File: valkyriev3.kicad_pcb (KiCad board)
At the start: 4 copper layers, 70 x 100 mm, 126 parts, among them J1 USB_C_Receptacle_USB2.0_16P, J10 Conn_01x03, J11 Conn_01x03, J2 DE9_Pins_MountingHoles, J3 SMA_180C, J4 SMA_180C, J5 Conn_01x02_Socket, J6 Conn_01x02_Socket, J7 Conn_01x02_Socket, J8 Conn_01x03, J9 Conn_01x05, Q1 BC817, Q2 BC817, Q3 BC817, Q4 BC817, Q5 BC817, Q6 DMG3420U, Q7 DMP2305U, Q8 DMG3420U, SW1 SW_SPST, SW2 SW_SPST, U1 W25Q128JVS, U10 LPS22HB, U2 ESP32-S3-MINI-1U, U3 MAX3232, U4 AMS1117-3.3, U5 TPS562202, U9 MS5607-02BA

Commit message: did some clean-up, did some to-do tasks.
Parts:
- added D1: S2A, Diode_SMD:D_SMB, B.Cu at (110.5, 89.7)
- added Q6: BC817, Package_TO_SOT_SMD:SOT-23, F.Cu at (136.5, 88.1)
- added Q7: BC817, Package_TO_SOT_SMD:SOT-23, F.Cu at (134.9, 91.5)
- added R24: 1k, Resistor_SMD:R_0603_1608Metric, F.Cu at (137.0, 85.6)
- added R25: 1k, Resistor_SMD:R_0603_1608Metric, F.Cu at (133.8, 87.9)
- added R26: 1k, Resistor_SMD:R_0603_1608Metric, F.Cu at (137.6, 91.3)
- added R27: 1k, Resistor_SMD:R_0603_1608Metric, F.Cu at (132.2, 90.5)
- moved J4 16.0 mm to (162.0, 114.1)
- moved J9 4.45 mm to (136.0, 95.2)
- renumbered D9 to D10, D10 to D11, D11 to D12, D1 to D2, D2 to D3, D3 to D4, D4 to D5, D5 to D6, D6 to D7, D7 to D8, D8 to D9, Q8 to Q10, Q6 to Q8, Q7 to Q9, R24 to R28, R25 to R29, R26 to R30, R27 to R31, R28 to R32
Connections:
- J1 pad A4: +5V -> /MCU/USB_VBUS
- J1 pad A9: +5V -> /MCU/USB_VBUS
- J1 pad B4: +5V -> /MCU/USB_VBUS
- J1 pad B9: +5V -> /MCU/USB_VBUS
- U2 pad 19: LORA_M0 -> LORA_M1
- U2 pad 20: LORA_M1 -> LORA_M0
- U2 pad 36: ESP_TXD2 -> ESP_RXD2
- U2 pad 37: ESP_RXD2 -> ESP_TXD2
- U8 pad 4: ESP_TXD1 -> ESP_RXD1
- U8 pad 5: ESP_RXD1 -> ESP_TXD1
- U8 pad 6: LORA_M0 -> /Communications/LORA_M1_C
- U8 pad 7: LORA_M1 -> /Communications/LORA_M0_C
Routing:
- net /MCU/USB_VBUS: track 0.00 -> 17.9 mm, vias 0 -> 8
- net +5V: track 92.3 -> 74.8 mm, vias 23 -> 15
- net /Communications/LORA_ANT: track 6.85 -> 20.5 mm
- net ESP_RXD1: track 50.6 -> 62.7 mm
- net LORA_M0: track 31.2 -> 20.7 mm, vias 2 -> 0
- net /Communications/LORA_M0_C: track 0.00 -> 10.3 mm
- net ESP_TXD1: track 50.3 -> 57.3 mm
- net /Communications/LORA_M1_C: track 0.00 -> 6.42 mm
- net LORA_M1: track 30.2 -> 24.2 mm, vias 2 -> 0
- net +3V3: track 38.8 -> 41.3 mm, vias 62 -> 64
- net /Communications/LORA_M0_B: track 0.00 -> 2.11 mm
- net /Communications/LORA_M1_B: track 0.00 -> 1.81 mm
- net ESP_RXD2: track 44.8 -> 44.5 mm, vias 2 -> 0
- net GND: vias 379 -> 398

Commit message: improvements, re-did some tasks. updated step file.
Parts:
- D1: value S2A -> 1N4007; footprint Diode_SMD:D_SMB -> Diode_THT:D_DO-41_SOD81_P2.54mm_Vertical_AnodeUp; moved to F.Cu
- moved G*** 2.74 mm to (153.3, 114.0)
- moved D1 0.77 mm to (109.7, 89.6)
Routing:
- net +5V: track 74.8 -> 78.6 mm
- net BUZZER: track 16.2 -> 18.1 mm
- net /MCU/ESP_BOOT: track 17.2 -> 18.5 mm
- net /MCU/USB_VBUS: track 17.9 -> 17.0 mm
- net GND: vias 398 -> 397
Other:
- board text added: "Designed By S. KÖMÜRCÜOĞLU"
- board text added: "GUNALTAY ROCKET TEAM Valkyrie V3.1 Flight Computer"
- board text added: "GUNALTAY ROCKET TEAM Valkyrie V3.1 Flight Computer Drawn By: S. KÖMÜRCÜOĞLU Reviewed By: Ö.T. ÖNSOY VIN: 7-15V DC"
- board text removed: "Drawn by S. KÖMÜRCÜOĞLU"
- board text removed: "GUNALTAY ROCKET TEAM Valkyrie V3 Flight Computer"
- board text removed: "GUNALTAY ROCKET TEAM Valkyrie V3 Flight Computer Drawn By: S. KÖMÜRCÜOĞLU Reviewed By: Ö.T. ÖNSOY VIN: 7-15V DC"

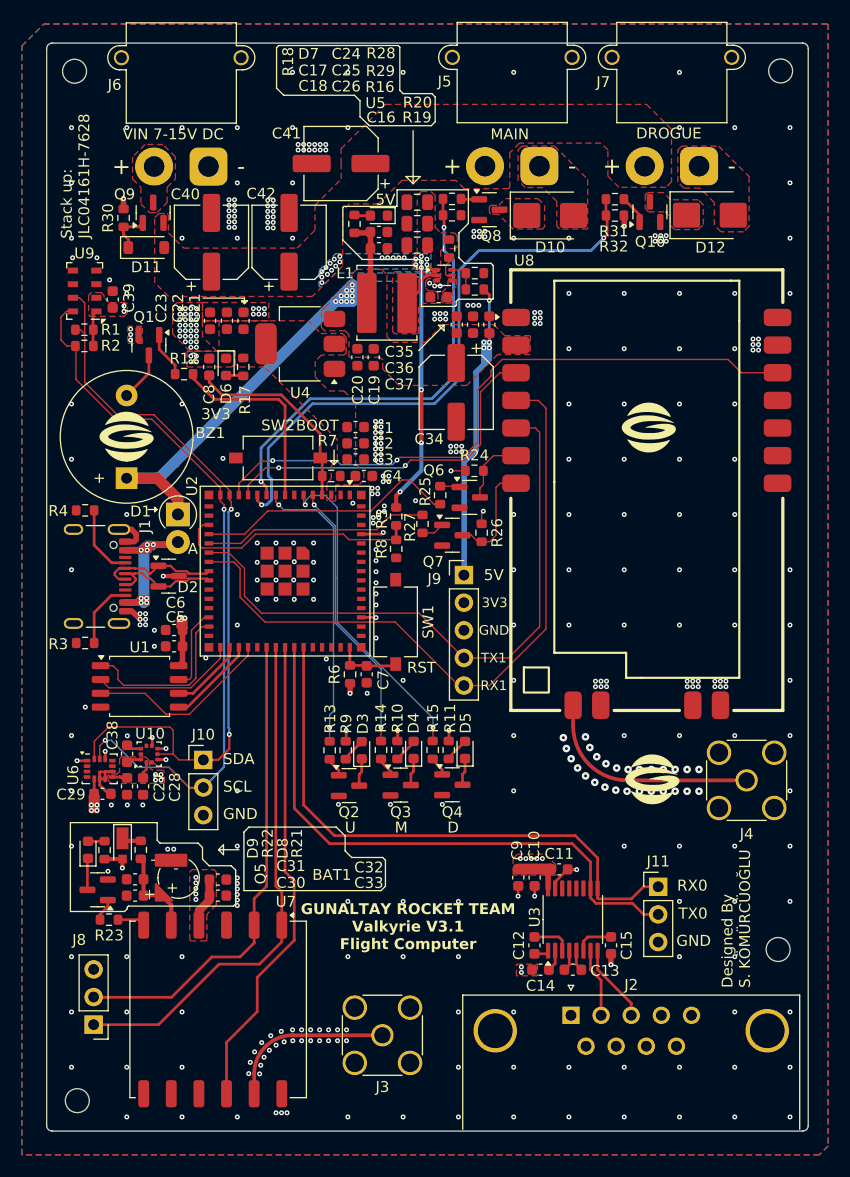
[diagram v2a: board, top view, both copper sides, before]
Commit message: Added more graphics, removed some unnecessary features. moved GPU passive components upper. added switching components to LoRa.
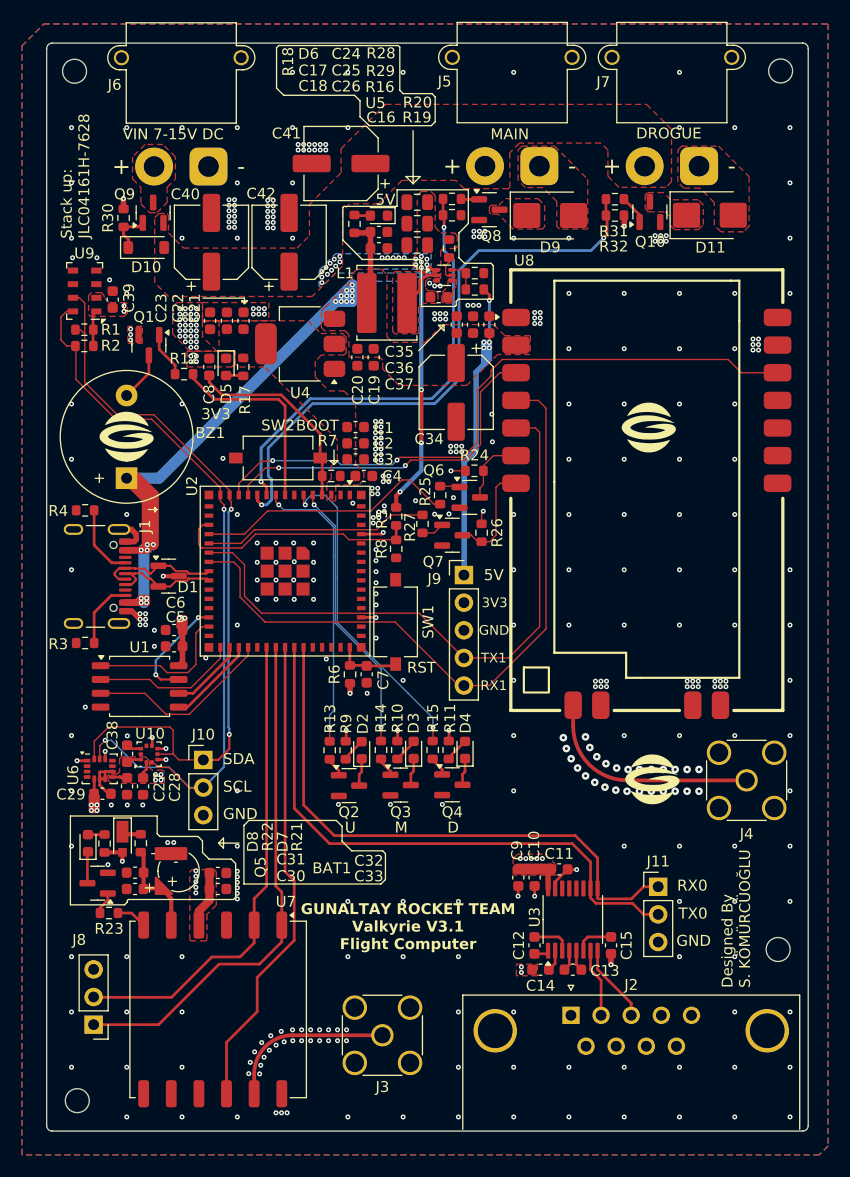
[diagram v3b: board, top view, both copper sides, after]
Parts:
- removed the D1 at (109.7, 89.6)
- added G***: LOGO, LOGO, B.Cu at (119.6, 71.1)
- added G***: LOGO, LOGO, B.Cu at (150.2, 63.8)
- moved G*** 34.9 mm to (140.2, 106.6)
- moved G*** 9.77 mm to (134.7, 125.1)
- moved G*** 9.77 mm to (145.7, 124.9)
- moved BAT1 0.61 mm to (109.8, 122.4)
- moved C30 0.61 mm to (105.8, 124.1)
- moved C31 0.61 mm to (105.8, 122.6)
- moved C32 0.61 mm to (113.4, 122.6)
- moved C33 0.61 mm to (113.4, 124.1)
- moved D7 0.61 mm to (104.6, 119.7)
- moved D8 0.61 mm to (101.4, 119.8)
- moved Q5 0.61 mm to (102.3, 123.5)
- moved R21 0.61 mm to (106.3, 119.8)
- moved R22 0.61 mm to (103.0, 119.9)
- moved R23 0.61 mm to (103.4, 126.3)
- renumbered D2 to D1, D11 to D10, D12 to D11, D3 to D2, D4 to D3, D5 to D4, D6 to D5, D7 to D6, D8 to D7, D9 to D8, D10 to D9
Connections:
- J1 pad A4: /MCU/USB_VBUS -> +5V
- J1 pad A9: /MCU/USB_VBUS -> +5V
- J1 pad B4: /MCU/USB_VBUS -> +5V
- J1 pad B9: /MCU/USB_VBUS -> +5V
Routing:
- net +5V: track 78.6 -> 100.9 mm, vias 15 -> 23
- net /MCU/USB_VBUS: track 17.0 -> 0.00 mm, vias 8 -> 0
- net SPI_HOLD: track 7.68 -> 10.1 mm, vias 0 -> 2
- net SPI_CS1: track 16.3 -> 14.1 mm
- net /GPS/GPS_VBCKP: track 8.18 -> 8.79 mm
- net +3V3: track 41.3 -> 41.9 mm
- net GND: vias 397 -> 402
